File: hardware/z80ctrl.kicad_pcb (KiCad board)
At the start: 2 copper layers, 99.8 x 49.9 mm, 29 parts, among them J1 BUS, J2 BUSEXT, J3 ISP, J4 RST/HALT, J5 S2 S1, J6 LINK, J7 Pololu SD, J8 Adafruit SD, J9 CLK/WAIT, SW1 RESET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

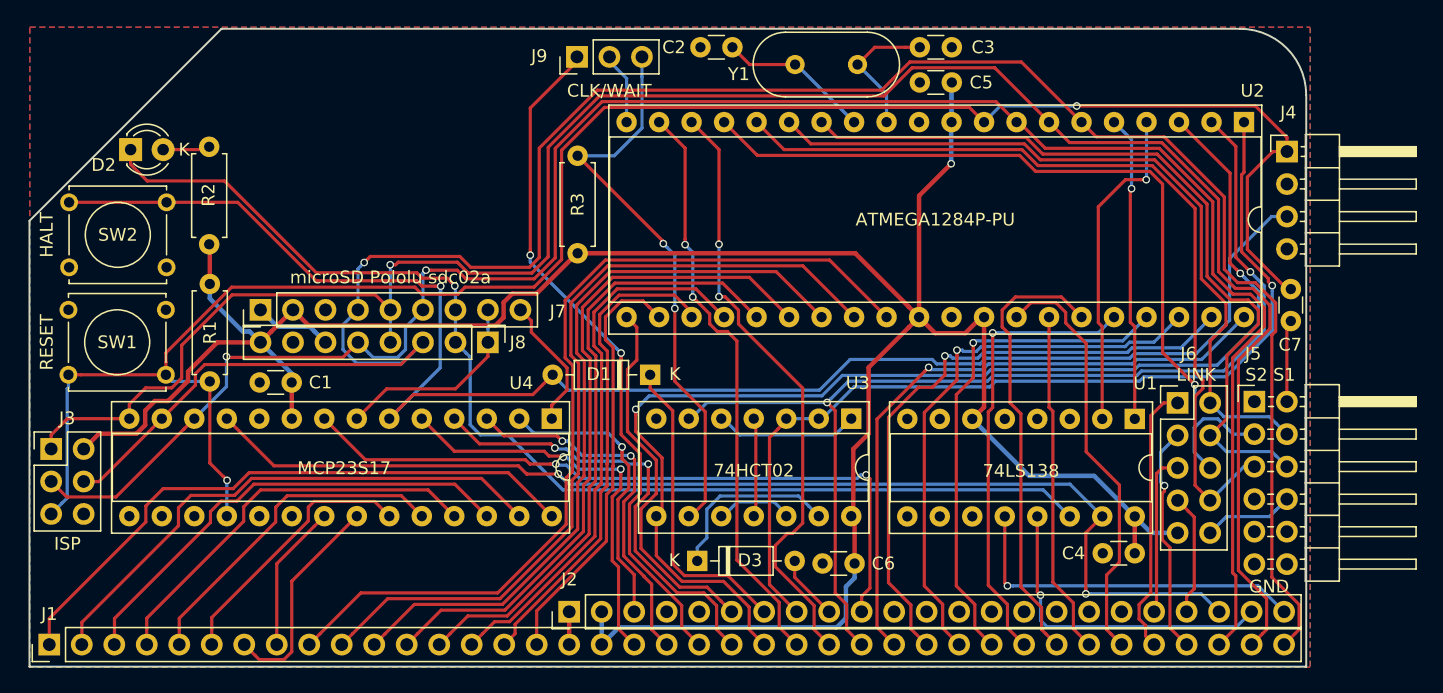
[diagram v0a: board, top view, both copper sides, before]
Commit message: Add era and cd commands; add hidden commands (not shown in help)
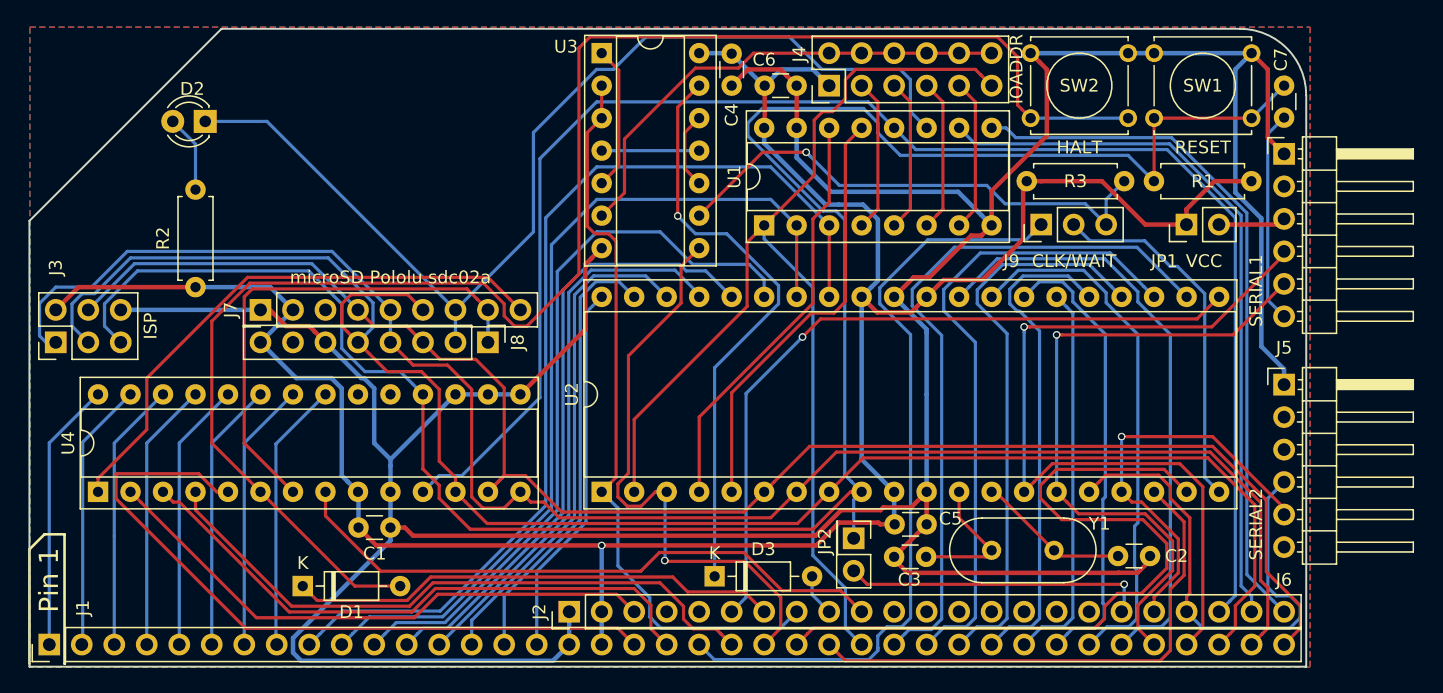
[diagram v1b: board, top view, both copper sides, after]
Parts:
- added JP1: VCC, Connector_PinHeader_2.54mm:PinHeader_1x02_P2.54mm_Vertical, F.Cu at (244.6, 118.8)
- added JP2: Jumper, Connector_PinHeader_2.54mm:PinHeader_2x01_P2.54mm_Vertical, F.Cu at (218.6, 143.3)
- J4: value RST/HALT -> IOADDR; footprint Connector_PinHeader_2.54mm:PinHeader_1x04_P2.54mm_Horizontal -> Connector_PinHeader_2.54mm:PinHeader_2x06_P2.54mm_Vertical
- J5: value S2 S1 -> SERIAL1; footprint Connector_PinHeader_2.54mm:PinHeader_2x06_P2.54mm_Horizontal -> Connector_PinHeader_2.54mm:PinHeader_1x06_P2.54mm_Horizontal
- J6: value LINK -> SERIAL2; footprint Connector_PinHeader_2.54mm:PinHeader_2x05_P2.54mm_Vertical -> Connector_PinHeader_2.54mm:PinHeader_1x06_P2.54mm_Horizontal
- U1: value 74LS138 -> 74HCT139
- moved SW1 87.2 mm to (242.1, 105.4)
- moved R1 81.8 mm to (249.7, 115.4), turned to 180 degrees
- moved SW2 76.1 mm to (232.4, 105.4)
- moved U2 57.9 mm to (198.9, 139.7), turned to 90 degrees
- moved C4 50.2 mm to (209.0, 105.5), turned to 270 degrees
- moved C2 49.9 mm to (239.2, 144.7), turned to 0 degrees
- moved Y1 43.0 mm to (234.2, 144.3), turned to 180 degrees
- moved C3 39.8 mm to (224.2, 144.8), turned to 180 degrees
- moved J9 38.6 mm to (233.2, 118.8)
- moved C6 38.0 mm to (211.6, 108.0), turned to 0 degrees
- moved J4 36.2 mm to (216.7, 108.0), turned to 90 degrees
- moved U4 35.9 mm to (159.5, 139.7), turned to 90 degrees
- moved R3 35.6 mm to (232.1, 115.4), turned to 0 degrees
- moved C5 34.8 mm to (221.8, 142.2), turned to 0 degrees
- moved U3 34.6 mm to (198.9, 105.4), turned to 0 degrees
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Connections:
- J1 pad 35: Net-(J1-Pad35) -> /TX
- J1 pad 36: Net-(J1-Pad36) -> /RX
- J2 pad 18: (no net) -> Net-(J2-Pad18)
- J2 pad 19: Net-(J2-Pad19) -> /TX2
- J2 pad 20: Net-(J2-Pad20) -> /RX2
- J4 pad 1: /~AVRRST~ -> VCC
- J4 pad 2: GND -> Net-(J4-Pad10)
- J4 pad 3: Net-(D1-Pad2) -> Net-(J4-Pad3)
- J4 pad 4: GND -> Net-(J4-Pad10)
- J5 pad 1: (no net) -> GND
- J5 pad 2: Net-(C7-Pad1) -> (no net)
- J5 pad 3: /TX2 -> Net-(J5-Pad3)
- J5 pad 4: /TX -> /RX
- J5 pad 5: /RX2 -> /TX
- J5 pad 6: /RX -> Net-(C7-Pad1)
- J6 pad 1: Net-(J1-Pad35) -> GND
- J6 pad 2: /TX -> (no net)
- J6 pad 3: Net-(J1-Pad36) -> (no net)
- J6 pad 4: /RX -> /RX2
- J6 pad 5: Net-(J2-Pad19) -> /TX2
- J6 pad 6: /TX2 -> (no net)
- SW2 pad 1: Net-(D1-Pad2) -> GND
- SW2 pad 2: GND -> Net-(D1-Pad2)
- U1 pad 1: /SPIA1 -> /~IORQ~
- U1 pad 10: (no net) -> /~AUXCS1~
- U1 pad 11: (no net) -> /~SDCS~
- U1 pad 12: /~AUXCS2~ -> /~IOXCS~
- U1 pad 13: /~AUXCS1~ -> /SPIA1
- U1 pad 14: /~SDCS~ -> /SPIA0
- U1 pad 15: /~IOXCS~ -> GND
- U1 pad 2: /SPIA0 -> /A6
- U1 pad 3: GND -> /A7
- U1 pad 4: GND -> Net-(J4-Pad3)
- U1 pad 5: GND -> Net-(J4-Pad5)
- U1 pad 6: VCC -> Net-(J4-Pad7)
- U1 pad 7: (no net) -> Net-(J4-Pad9)
- U1 pad 9: (no net) -> /~AUXCS2~
- U2 pad 22: /A0 -> /D0
- U2 pad 23: /A1 -> /D1
- U2 pad 24: /A2 -> /D2
- U2 pad 25: /A3 -> /D3
- U2 pad 26: /A4 -> /D4
- U2 pad 27: /A5 -> /D5
- U2 pad 28: /A6 -> /D6
- U2 pad 29: /A7 -> /D7
- U2 pad 33: /D7 -> /A7
- U2 pad 34: /D6 -> /A6
- U2 pad 35: /D5 -> /A5
- U2 pad 36: /D4 -> /A4
- U2 pad 37: /D3 -> /A3
- U2 pad 38: /D2 -> /A2
- U2 pad 39: /D1 -> /A1
- U2 pad 40: /D0 -> /A0
- U3 pad 6: /~IORQ~ -> Net-(J4-Pad10)
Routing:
- net GND: track 8.70 -> 296.2 mm
- net /~MREQ~: track 94.6 -> 46.6 mm, vias 2 -> 1
- net /MOSI: track 169.2 -> 126.0 mm, vias 1 -> 0
- net Net-(J4-Pad10): track 0.00 -> 38.2 mm
- net /SDEN: track 10.5 -> 44.5 mm
- net /TX2: track 65.5 -> 32.1 mm
- net /~IOXCS~: track 89.2 -> 122.1 mm, vias 2 -> 0
- net Net-(D3-Pad1): track 14.2 -> 45.8 mm, vias 0 -> 1
- net /~AUXCS1~: track 25.4 -> 56.2 mm, vias 1 -> 0
- net /MISO: track 161.7 -> 132.9 mm, vias 1 -> 0
- net /~BUSACK~: track 29.3 -> 57.6 mm, vias 0 -> 1
- net /~AUXCS2~: track 28.0 -> 55.1 mm, vias 1 -> 0
- net /A15: track 48.2 -> 21.1 mm
- net /RX2: track 65.4 -> 40.4 mm
- net /~M1~: track 31.9 -> 56.5 mm, vias 2 -> 0
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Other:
- board text added: "J4: IO addresses - None (left) - 00-3F - 40-7F - 80-BF - C0-FF - 00-FF (right) JP1: VCC from SERIAL1 JP2: VCC from SERIAL2"
- board text added: "Pin 1"
- board text added: "z80ctrl REV4 (C)2018 J.B. Langston https://github.com/jblang/z80ctrl"
- board text removed: "GND"
- board text removed: "J6 Link Jumpers (top to bottom): TX RX TX2 RX2 VCC from Serial"
- board text removed: "K"
- board text removed: "z80ctrl REV5 (C)2018 J.B. Langston https://github.com/jblang/z80ctrl"

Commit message: Update silkscreen
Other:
- board text added: "J4: IO addresses - None (left) - 00-3F - 40-7F - 80-BF - C0-FF - 00-FF (right) JP1: VCC from SERIAL1 JP2: RESET for IO expander"
- board text removed: "J4: IO addresses - None (left) - 00-3F - 40-7F - 80-BF - C0-FF - 00-FF (right) JP1: VCC from SERIAL1 JP2: VCC from SERIAL2"
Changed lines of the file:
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@@
     (effects (font (size 1 1) (thickness 0.15)))
   )
-  (gr_text "J4: IO addresses\n- None (left)\n- 00-3F\n- 40-7F\n- 80-BF\n- C0-FF\n- 00-FF (right)\n\nJP1: VCC from SERIAL1\nJP2: VCC from SERIAL2" (at 194.31 113.03) (layer B.SilkS)
+  (gr_text "J4: IO addresses\n- None (left)\n- 00-3F\n- 40-7F\n- 80-BF\n- C0-FF\n- 00-FF (right)\n\nJP1: VCC from SERIAL1\nJP2: RESET for IO expander" (at 194.31 113.03) (layer B.SilkS)
     (effects (font (size 1 1) (thickness 0.15)) (justify left mirror))
   )

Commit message: Updates for REV5
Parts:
- added JP3: HALT, Connector_PinHeader_2.54mm:PinHeader_1x02_P2.54mm_Vertical, F.Cu at (156.0, 141.9)
- added JP4: RST, Connector_PinHeader_2.54mm:PinHeader_1x02_P2.54mm_Vertical, F.Cu at (156.0, 133.0)
- moved D1 6.54 mm to (169.7, 144.1)
- moved SW2 1.31 mm to (232.4, 106.7)
- moved SW1 1.31 mm to (242.1, 106.7)
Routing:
- net Net-(D1-Pad2): track 128.2 -> 150.1 mm
- net GND: track 296.2 -> 312.6 mm
- net /~M1~: track 56.5 -> 42.2 mm, vias 0 -> 1
- net /~AVRRST~: track 169.3 -> 176.2 mm
- net /~HALT~: track 38.4 -> 44.0 mm
- net /~NMI~: track 48.1 -> 46.9 mm
- net /~INT~: track 49.8 -> 50.6 mm
- net /~RFSH~: track 44.8 -> 44.2 mm
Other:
- board text added: "K"
- board text added: "z80ctrl REV5 (C)2018 J.B. Langston https://github.com/jblang/z80ctrl"
- board text removed: "Pin 1"
- board text removed: "z80ctrl REV4 (C)2018 J.B. Langston https://github.com/jblang/z80ctrl"

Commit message: REV5 tweaks
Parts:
- removed JP1: VCC, Connector_PinHeader_2.54mm:PinHeader_1x02_P2.54mm_Vertical
- removed JP2: Jumper, Connector_PinHeader_2.54mm:PinHeader_2x01_P2.54mm_Vertical
- removed JP3: HALT, Connector_PinHeader_2.54mm:PinHeader_1x02_P2.54mm_Vertical
- removed JP4: RST, Connector_PinHeader_2.54mm:PinHeader_1x02_P2.54mm_Vertical
- J4: value IOADDR -> RST/HALT; footprint Connector_PinHeader_2.54mm:PinHeader_2x06_P2.54mm_Vertical -> Connector_PinHeader_2.54mm:PinHeader_1x04_P2.54mm_Horizontal
- J5: value SERIAL1 -> S2 S1; footprint Connector_PinHeader_2.54mm:PinHeader_1x06_P2.54mm_Horizontal -> Connector_PinHeader_2.54mm:PinHeader_2x06_P2.54mm_Horizontal
- J6: value SERIAL2 -> LINK; footprint Connector_PinHeader_2.54mm:PinHeader_1x06_P2.54mm_Horizontal -> Connector_PinHeader_2.54mm:PinHeader_2x05_P2.54mm_Vertical
- U1: value 74HCT139 -> 74LS138
- moved SW1 86.9 mm to (157.2, 125.5)
- moved R1 81.8 mm to (168.2, 123.5), turned to 270 degrees
- moved SW2 75.8 mm to (157.2, 117.1)
- moved U2 57.9 mm to (249.1, 110.8), turned to 270 degrees
- moved C4 50.2 mm to (240.6, 144.5), turned to 180 degrees
- moved C2 49.9 mm to (209.1, 105.0), turned to 180 degrees
- moved Y1 43.0 mm to (214.0, 106.3), turned to 0 degrees
- moved C3 39.8 mm to (223.8, 105.0), turned to 0 degrees
- moved J9 38.6 mm to (196.9, 105.7)
- moved C6 37.2 mm to (218.5, 144.6), turned to 180 degrees
- moved J4 36.2 mm to (252.4, 113.1), turned to 0 degrees
- moved U4 35.9 mm to (195.0, 134.0), turned to 270 degrees
- moved D1 35.7 mm to (202.7, 130.6), turned to 180 degrees
- moved R3 35.6 mm to (197.0, 121.0), turned to 90 degrees
- moved C5 34.8 mm to (226.2, 107.7), turned to 180 degrees
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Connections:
- J1 pad 35: /TX -> Net-(J1-Pad35)
- J1 pad 36: /RX -> Net-(J1-Pad36)
- J2 pad 18: Net-(J2-Pad18) -> (no net)
- J2 pad 19: /TX2 -> Net-(J2-Pad19)
- J2 pad 20: /RX2 -> Net-(J2-Pad20)
- J4 pad 1: VCC -> /~AVRRST~
- J4 pad 2: Net-(J4-Pad10) -> GND
- J4 pad 3: Net-(J4-Pad3) -> Net-(D1-Pad2)
- J4 pad 4: Net-(J4-Pad10) -> GND
- J5 pad 1: GND -> (no net)
- J5 pad 2: (no net) -> Net-(C7-Pad1)
- J5 pad 3: Net-(J5-Pad3) -> /TX2
- J5 pad 4: /RX -> /TX
- J5 pad 5: /TX -> /RX2
- J5 pad 6: Net-(C7-Pad1) -> /RX
- J6 pad 1: GND -> Net-(J1-Pad35)
- J6 pad 2: (no net) -> /TX
- J6 pad 3: (no net) -> Net-(J1-Pad36)
- J6 pad 4: /RX2 -> /RX
- J6 pad 5: /TX2 -> Net-(J2-Pad19)
- J6 pad 6: (no net) -> /TX2
- SW2 pad 1: GND -> Net-(D1-Pad2)
- SW2 pad 2: Net-(D1-Pad2) -> GND
- U1 pad 1: /~IORQ~ -> /SPIA1
- U1 pad 10: /~AUXCS1~ -> (no net)
- U1 pad 11: /~SDCS~ -> (no net)
- U1 pad 12: /~IOXCS~ -> /~AUXCS2~
- U1 pad 13: /SPIA1 -> /~AUXCS1~
- U1 pad 14: /SPIA0 -> /~SDCS~
- U1 pad 15: GND -> /~IOXCS~
- U1 pad 2: /A6 -> /SPIA0
- U1 pad 3: /A7 -> GND
- U1 pad 4: Net-(J4-Pad3) -> GND
- U1 pad 5: Net-(J4-Pad5) -> GND
- U1 pad 6: Net-(J4-Pad7) -> VCC
- U1 pad 7: Net-(J4-Pad9) -> (no net)
- U1 pad 9: /~AUXCS2~ -> (no net)
- U2 pad 22: /D0 -> /A0
- U2 pad 23: /D1 -> /A1
- U2 pad 24: /D2 -> /A2
- U2 pad 25: /D3 -> /A3
- U2 pad 26: /D4 -> /A4
- U2 pad 27: /D5 -> /A5
- U2 pad 28: /D6 -> /A6
- U2 pad 29: /D7 -> /A7
- U2 pad 33: /A7 -> /D7
- U2 pad 34: /A6 -> /D6
- U2 pad 35: /A5 -> /D5
- U2 pad 36: /A4 -> /D4
- U2 pad 37: /A3 -> /D3
- U2 pad 38: /A2 -> /D2
- U2 pad 39: /A1 -> /D1
- U2 pad 40: /A0 -> /D0
- U3 pad 6: Net-(J4-Pad10) -> /~IORQ~
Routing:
- net GND: track 312.6 -> 8.70 mm
- net /~MREQ~: track 46.4 -> 94.5 mm, vias 1 -> 2
- net /MOSI: track 126.0 -> 169.2 mm, vias 0 -> 1
- net VCC: track 188.9 -> 230.7 mm, vias 1 -> 0
- net Net-(J4-Pad10): track 38.2 -> 0.00 mm
- net Net-(D3-Pad1): track 45.8 -> 11.2 mm, vias 1 -> 0
- net /SDEN: track 44.5 -> 10.5 mm
- net /TX2: track 32.1 -> 65.5 mm
- net /~IOXCS~: track 122.1 -> 89.2 mm, vias 0 -> 2
- net /~AUXCS1~: track 56.2 -> 25.4 mm, vias 0 -> 1
- net /MISO: track 132.9 -> 161.7 mm, vias 0 -> 1
- net /~BUSACK~: track 57.6 -> 29.3 mm, vias 1 -> 0
- net /~AUXCS2~: track 55.1 -> 27.4 mm, vias 0 -> 1
- net /A15: track 21.1 -> 48.2 mm
- net Net-(D1-Pad2): track 150.1 -> 124.4 mm, vias 0 -> 1
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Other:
- board text removed: "J4: IO addresses - None (left) - 00-3F - 40-7F - 80-BF - C0-FF - 00-FF (right) JP1: VCC from SERIAL1 JP2: RESET for IO expander"

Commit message: Add legend for LINK header to back silkscreen
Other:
- board text added: "GND"
- board text added: "J6 Link Jumpers (top to bottom): TX RX TX2 RX2 VCC from Serial"
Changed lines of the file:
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@@
   (general
     (thickness 1.6)
-    (drawings 9)
+    (drawings 11)
     (tracks 997)
     (zones 0)
@@
       (rotate (xyz 0 0 0))
     )
+  )
+  (gr_text "J6 Link Jumpers \n(top to bottom):\nTX\nRX\nTX2\nRX2\nVCC from Serial" (at 193 113.95) (layer B.SilkS)
+    (effects (font (size 1.5 1.5) (thickness 0.3)) (justify left mirror))
+  )
+  (gr_text GND (at 251.05 147.1) (layer F.SilkS)
+    (effects (font (size 1 1) (thickness 0.15)))
   )
   (gr_text "z80ctrl REV5\n(C)2018 J.B. Langston\nhttps://github.com/jblang/z80ctrl" (at 225.5 118.9) (layer B.SilkS)
@@
     (connect_pads (clearance 0.508))
     (min_thickness 0.254)
-    (fill (arc_segments 16) (thermal_gap 0.508) (thermal_bridge_width 0.508))
+    (fill yes (arc_segments 16) (thermal_gap 0.508) (thermal_bridge_width 0.508))
     (polygon
       (pts
@@
     (connect_pads (clearance 0.508))
     (min_thickness 0.254)
-    (fill (arc_segments 16) (thermal_gap 0.508) (thermal_bridge_width 0.508))
+    (fill yes (arc_segments 16) (thermal_gap 0.508) (thermal_bridge_width 0.508))
     (polygon
       (pts

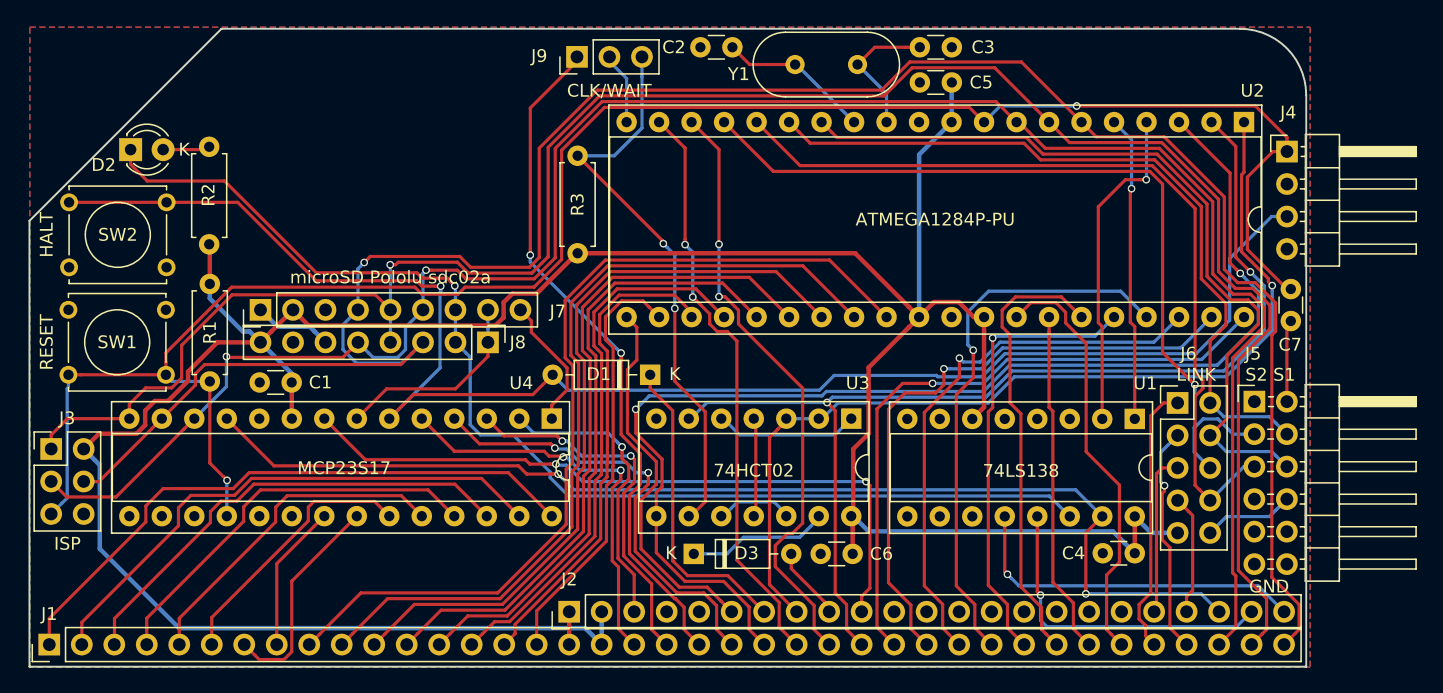
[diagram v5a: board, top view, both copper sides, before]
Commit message: Fix breaks in groundplane
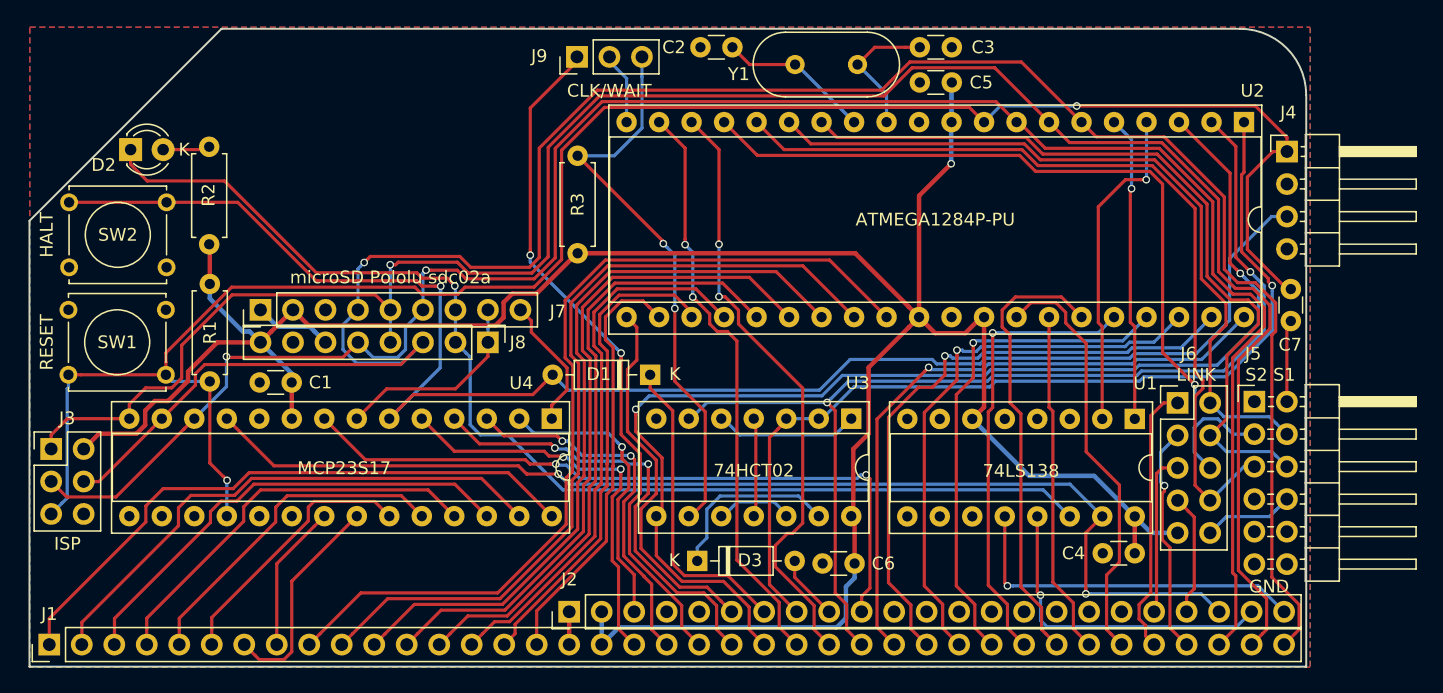
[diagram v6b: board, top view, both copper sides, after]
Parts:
- moved C6 0.76 mm to (218.7, 145.3)
- moved D3 0.61 mm to (206.3, 145.1)
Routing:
- net VCC: track 230.7 -> 198.3 mm, vias 0 -> 1
- net /D3: track 43.3 -> 39.7 mm
- net Net-(D3-Pad1): track 11.2 -> 14.2 mm
- net /~WAIT~: track 5.75 -> 5.09 mm
- net /~NMI~: track 55.0 -> 55.5 mm
- net /~AUXCS2~: track 27.4 -> 28.0 mm
